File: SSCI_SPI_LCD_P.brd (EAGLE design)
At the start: 114 x 100 mm, 116 parts, among them IC13 74LVC541_RGY, IC18 74LVC541_RGY, IC3 74LVC541_RGY, IC8 74LVC541_RGY, X1 TSW-108-02-S-S, X2 TSW-108-02-S-S, X3 TSW-108-02-S-S, X4 TSW-108-02-S-S, X5 TSW-108-02-S-S, X6 TSW-108-02-S-S, X7 TSW-108-02-S-S, X8 TSW-108-02-S-S

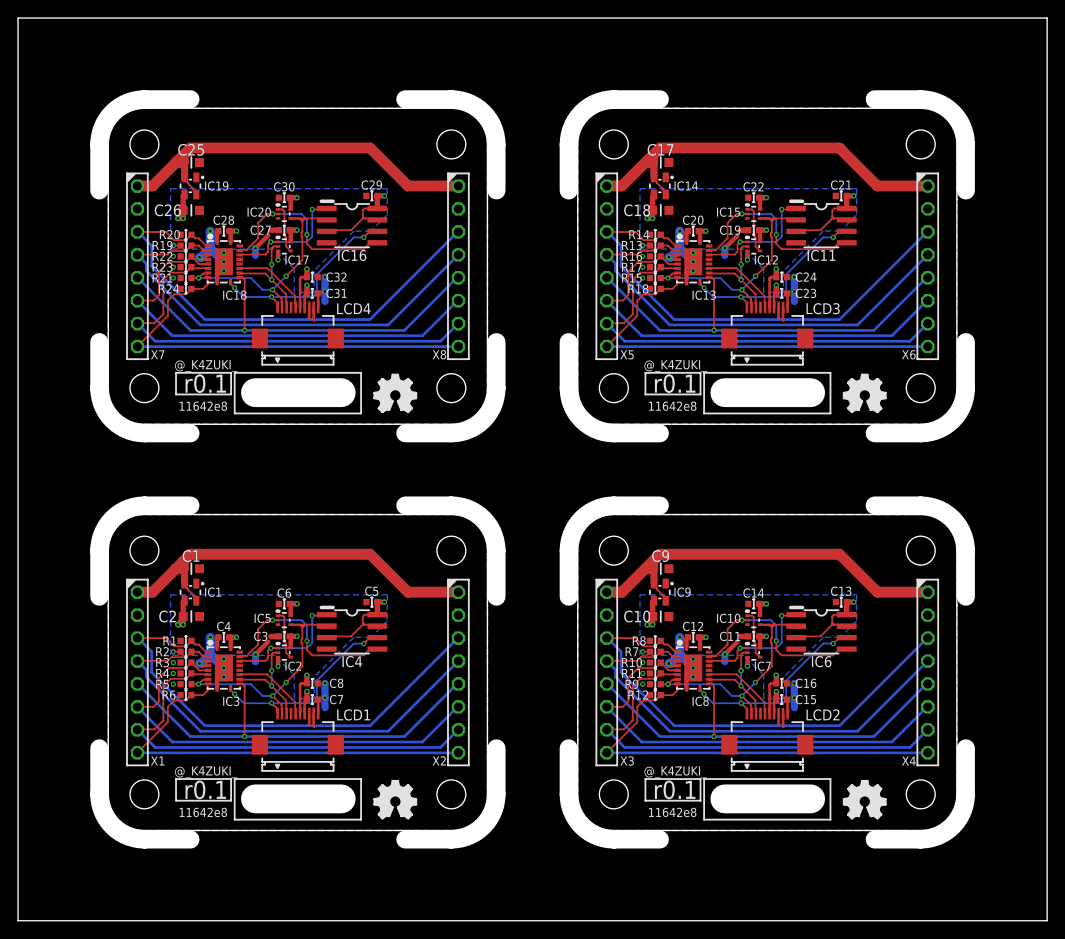
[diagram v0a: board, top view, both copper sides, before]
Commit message: apply changes to panelising file
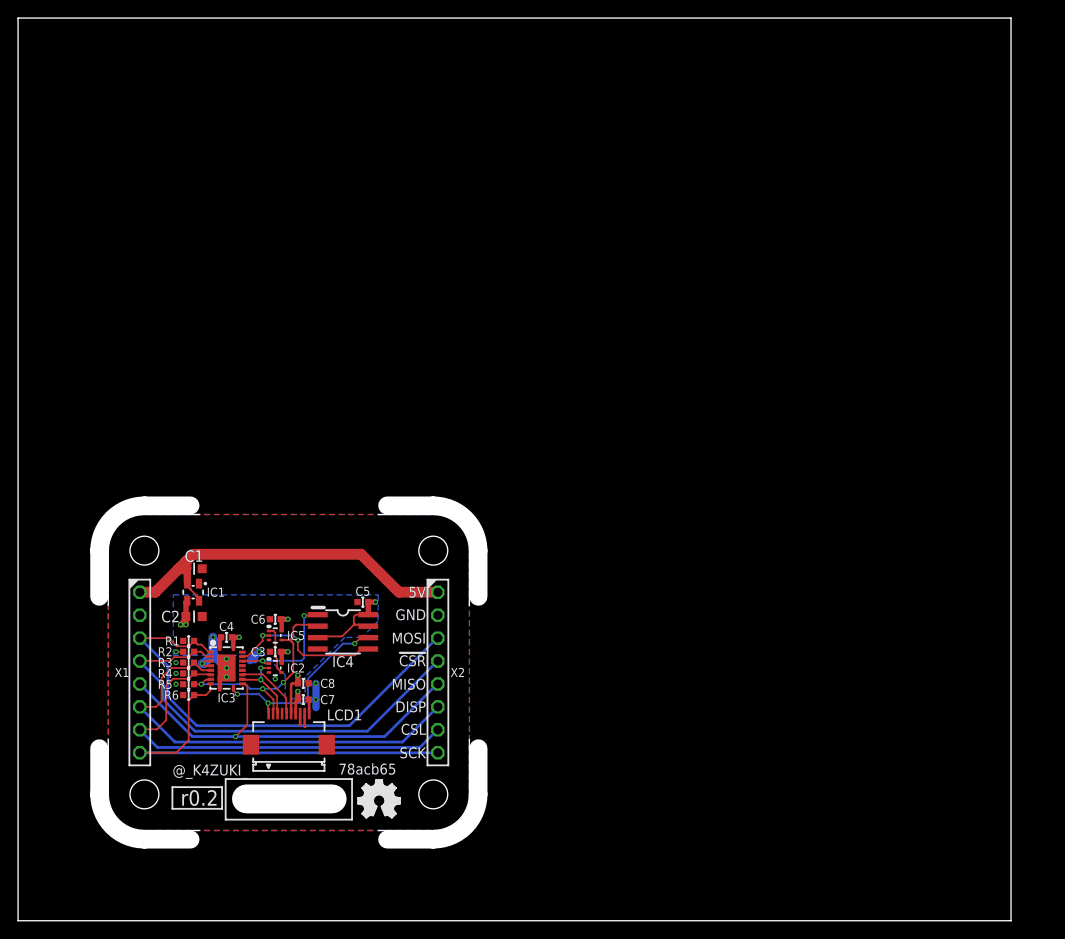
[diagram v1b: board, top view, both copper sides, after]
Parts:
- removed C10, C17, C18, C25, C26, C9: (no value), mylib:CR_1608
- removed C11, C12, C13, C14, C15, C16, C19, C20, C21, C22, C23, C24, C27, C28, C29, C30, C31, C32, R10, R11, R12, R13, R14, R15, R16, R17, R18, R19, R20, R21, R22, R23, R24, R7, R8, R9: (no value), mylib:C0402
- removed GIT2, GIT3, GIT4: 11642e8, git-revision:GIT-REVISION
- removed IC10, IC12, IC15, IC17, IC20, IC7: (no value), mylib:SOT50P160X120-5N
- removed IC11, IC16, IC6: (no value), mylib:IC_08_1.27_150MIL
- removed IC13, IC18, IC8: 74LVC541_RGY, mylib:QFN50P460X360-20N
- removed IC14, IC19, IC9: (no value), mylib:SOT130P220X135-4N
- removed ICON3, ICON5, ICON7: r0.1, mylib:ICON_REVISION2.0
- removed ICON4, ICON6, ICON8: (no value), mylib:ICON_OSHW
- removed LCD2, LCD3, LCD4: LCD_GLCD_400X240, mylib:LCD_GLCD_400X240
- removed P10, P11, P12, P13, P14, P15, P16, P5, P6, P7, P8, P9: (no value), mylib:PCB_CORNER
- removed X3, X4, X5, X6, X7, X8: TSW-108-02-S-S, con-samtec.local:TSW-108-02-S-S
- GIT1: value 11642e8 -> 78acb65; device git-revision:GIT-REVISION -> git-revision:GIT-REVISION_1.2
- ICON1: value r0.1 -> r0.2; device mylib:ICON_REVISION2.0 -> mylib:ICON_REVISION1.7
- moved GIT1 18.8 mm to (38.7, 16.8)
- moved X2 2.27 mm to (46.5, 27.5)
- moved P1 2.00 mm to (46.0, 14.0)
- moved P2 2.00 mm to (46.0, 41.0)
- moved C6 1.97 mm to (28.5, 33.4)
- moved C3 1.97 mm to (28.5, 29.8)
- moved IC2 1.97 mm to (28.5, 28.0)
- moved IC5 1.97 mm to (28.5, 31.6)
- moved ICON2 1.80 mm to (40.0, 13.3)
- moved ICON1 1.08 mm to (20.2, 13.6)
- moved C5 1.00 mm to (38.2, 35.3)
- moved C7 1.00 mm to (31.6, 24.5)
- moved C8 1.00 mm to (31.6, 26.3)
- moved IC4 1.00 mm to (36.0, 32.0)
- moved LCD1 1.00 mm to (30.0, 19.5)
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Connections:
- removed net !CSR!-1: IC6.1, IC7.1, IC8.17
- removed net !CSR!-2: IC11.1, IC12.1, IC13.17
- removed net !CSR!-3: IC16.1, IC17.1, IC18.17
- removed net !CSR!1: IC8.3, R7.2, X3.4, X4.4
- removed net !CSR!2: IC13.3, R13.2, X5.4, X6.4
- removed net !CSR!3: IC18.3, R19.2, X7.4, X8.4
- removed net 3.3V1: C10.1, C11.1, C12.1, C13.1, C14.1, C15.1, C16.1, IC10.5, IC6.3, IC6.7, IC6.8, IC7.5, IC8.20, IC9.3, LCD2.6, LCD2.7, R7.1
- removed net 3.3V2: C18.1, C19.1, C20.1, C21.1, C22.1, C23.1, C24.1, IC11.3, IC11.7, IC11.8, IC12.5, IC13.20, IC14.3, IC15.5, LCD3.6, LCD3.7, R13.1
- removed net 3.3V3: C26.1, C27.1, C28.1, C29.1, C30.1, C31.1, C32.1, IC16.3, IC16.7, IC16.8, IC17.5, IC18.20, IC19.3, IC20.5, LCD4.6, LCD4.7, R19.1
- removed net 5V1: C9.1, IC9.2, IC9.4, X3.1, X4.1
- removed net 5V2: C17.1, IC14.2, IC14.4, X5.1, X6.1
- removed net 5V3: C25.1, IC19.2, IC19.4, X7.1, X8.1
- removed net CSL-1: IC7.2, IC8.13, LCD2.3
- removed net CSL-2: IC12.2, IC13.13, LCD3.3
- removed net CSL-3: IC17.2, IC18.13, LCD4.3
- removed net CSL1: IC8.7, R11.2, X3.7, X4.7
- removed net CSL2: IC13.7, R17.2, X5.7, X6.7
- removed net CSL3: IC18.7, R23.2, X7.7, X8.7
- removed net DISP-1: IC8.14, LCD2.5
- removed net DISP-2: IC13.14, LCD3.5
- removed net DISP-3: IC18.14, LCD4.5
- removed net DISP1: IC8.6, R10.2, X3.6, X4.6
- removed net DISP2: IC13.6, R16.2, X5.6, X6.6
- removed net DISP3: IC18.6, R22.2, X7.6, X8.6
- removed net GND1: C10.2, C11.2, C12.2, C13.2, C14.2, C15.2, C16.2, C9.2, IC10.3, IC6.4, IC7.3, IC8.1, IC8.10, IC8.19, IC8.4, IC8.5, IC8.EP, IC9.1, LCD2.10, LCD2.8, LCD2.9, LCD2.PAD1, LCD2.PAD2, R10.1, R11.1, R12.1, R8.1, R9.1, X3.2, X4.2
- removed net GND2: C17.2, C18.2, C19.2, C20.2, C21.2, C22.2, C23.2, C24.2, IC11.4, IC12.3, IC13.1, IC13.10, IC13.19, IC13.4, IC13.5, IC13.EP, IC14.1, IC15.3, LCD3.10, LCD3.8, LCD3.9, LCD3.PAD1, LCD3.PAD2, R14.1, R15.1, R16.1, R17.1, R18.1, X5.2, X6.2
- removed net GND3: C25.2, C26.2, C27.2, C28.2, C29.2, C30.2, C31.2, C32.2, IC16.4, IC17.3, IC18.1, IC18.10, IC18.19, IC18.4, IC18.5, IC18.EP, IC19.1, IC20.3, LCD4.10, LCD4.8, LCD4.9, LCD4.PAD1, LCD4.PAD2, R20.1, R21.1, R22.1, R23.1, R24.1, X7.2, X8.2
- removed net MISO-1: IC10.4, IC6.2, IC8.8, LCD2.2, R9.2
- removed net MISO-2: IC11.2, IC13.8, IC15.4, LCD3.2, R15.2
- removed net MISO-3: IC16.2, IC18.8, IC20.4, LCD4.2, R21.2
- removed net MISO1: IC8.12, X3.5, X4.5
- removed net MISO2: IC13.12, X5.5, X6.5
- removed net MISO3: IC18.12, X7.5, X8.5
- removed net MOSI-1: IC10.2, IC6.5, IC8.18
- removed net MOSI-2: IC11.5, IC13.18, IC15.2
- removed net MOSI-3: IC16.5, IC18.18, IC20.2
- removed net MOSI1: IC8.2, R8.2, X3.3, X4.3
- removed net MOSI2: IC13.2, R14.2, X5.3, X6.3
- removed net MOSI3: IC18.2, R20.2, X7.3, X8.3
- removed net N$1: IC10.1, IC7.4
- removed net N$3: IC12.4, IC15.1
- removed net N$4: IC17.4, IC20.1
- removed net SCK-1: IC6.6, IC8.11, LCD2.1
- removed net SCK-2: IC11.6, IC13.11, LCD3.1
- removed net SCK-3: IC16.6, IC18.11, LCD4.1
- removed net SCK1: IC8.9, R12.2, X3.8, X4.8
- removed net SCK2: IC13.9, R18.2, X5.8, X6.8
- removed net SCK3: IC18.9, R24.2, X7.8, X8.8
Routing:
- net MOSI1: track 54.0 -> 0.00 mm
- net MOSI3: track 54.0 -> 0.00 mm
- net MOSI2: track 54.0 -> 0.00 mm
- net !CSR!3: track 51.0 -> 0.00 mm
- net !CSR!1: track 51.0 -> 0.00 mm
- net !CSR!2: track 51.0 -> 0.00 mm
- net DISP3: track 50.6 -> 0.00 mm
- net DISP2: track 50.6 -> 0.00 mm
- net DISP1: track 50.6 -> 0.00 mm
- net CSL3: track 50.0 -> 0.00 mm
- net CSL2: track 50.0 -> 0.00 mm
- net CSL1: track 50.0 -> 0.00 mm
- net SCK3: track 48.0 -> 0.00 mm
- net SCK1: track 48.0 -> 0.00 mm
- net SCK2: track 48.0 -> 0.00 mm
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- removed copper zone on layer 16, net 3.3V1
- removed copper zone on layer 16, net 3.3V2
- removed copper zone on layer 16, net 3.3V3
- removed copper zone on layer 1, net GND1
- removed copper zone on layer 16, net GND1
- removed copper zone on layer 1, net GND2
- removed copper zone on layer 16, net GND2
- removed copper zone on layer 1, net GND3
- removed copper zone on layer 16, net GND3
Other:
- board size 114 x 100 mm -> 110 x 100 mm
- board text added: "!CSR!"
- board text added: "5V"
- board text added: "CSL"
- board text added: "DISP"
- board text added: "GND"
- board text added: "MISO"
- board text added: "MOSI"
- board text added: "SCK"
- board text removed: "C1"
- board text removed: "C2"
- board text removed: "C3"
- board text removed: "C4"
- board text removed: "C5"
- board text removed: "C6"
- board text removed: "C7"
- board text removed: "C8"
- board text removed: "IC1"
- board text removed: "IC2"
- board text removed: "IC3"
- board text removed: "IC4"
- board text removed: "IC5"
- board text removed: "LCD1"
- board text removed: "R1"
- board text removed: "R2"
- board text removed: "R3"
- board text removed: "R4"
- board text removed: "R5"
- board text removed: "R6"
- board text removed: "X1"
- board text removed: "X2"

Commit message: update libraries; update panelise; update gerbers
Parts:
- added C10, C17, C18, C25, C26, C9: (no value), mylib:CR_1608
- added C11, C12, C13, C14, C15, C16, C19, C20, C21, C22, C23, C24, C27, C28, C29, C30, C31, C32, R10, R11, R12, R13, R14, R15, R16, R17, R18, R19, R20, R21, R22, R23, R24, R7, R8, R9: (no value), mylib:C0402
- added GIT2, GIT3, GIT4: fd68d81, git-revision:GIT-REVISION_1.2
- added I1, I2, I3, I4: (no value), mylib:ICON_MINLAB_5.2MM
- added IC10, IC12, IC15, IC17, IC20, IC7: (no value), mylib:SOT50P160X120-5N
- added IC11, IC16, IC6: (no value), mylib:IC_08_1.27_150MIL
- added IC13, IC18, IC8: 74LVC541_RGY, mylib:QFN50P460X360-20N
- added IC14, IC19, IC9: (no value), mylib:SOT130P220X135-4N
- added ICON3, ICON5, ICON7: r0.2, mylib:ICON_REVISION1.7
- added ICON4, ICON6, ICON8: (no value), mylib:ICON_OSHW
- added LCD2, LCD3, LCD4: LCD_GLCD_400X240, mylib:LCD_GLCD_400X240
- added P10, P11, P12, P13, P14, P15, P16, P5, P6, P7, P8, P9: (no value), mylib:PCB_CORNER
- added X3, X4, X5, X6, X7, X8: TSW-108-02-S-S, con-samtec.local:TSW-108-02-S-S
- GIT1: value 78acb65 -> fd68d81
- moved ICON1 36.0 mm to (40.5, 43.3)
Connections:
- new net !CSR!-1: IC6.1, IC7.1, IC8.17
- new net !CSR!-2: IC11.1, IC12.1, IC13.17
- new net !CSR!-3: IC16.1, IC17.1, IC18.17
- new net !CSR!1: IC8.3, R7.2, X3.4, X4.4
- new net !CSR!2: IC13.3, R13.2, X5.4, X6.4
- new net !CSR!3: IC18.3, R19.2, X7.4, X8.4
- new net 3.3V1: C10.1, C11.1, C12.1, C13.1, C14.1, C15.1, C16.1, IC10.5, IC6.3, IC6.7, IC6.8, IC7.5, IC8.20, IC9.3, LCD2.6, LCD2.7, R7.1
- new net 3.3V2: C18.1, C19.1, C20.1, C21.1, C22.1, C23.1, C24.1, IC11.3, IC11.7, IC11.8, IC12.5, IC13.20, IC14.3, IC15.5, LCD3.6, LCD3.7, R13.1
- new net 3.3V3: C26.1, C27.1, C28.1, C29.1, C30.1, C31.1, C32.1, IC16.3, IC16.7, IC16.8, IC17.5, IC18.20, IC19.3, IC20.5, LCD4.6, LCD4.7, R19.1
- new net 5V1: C9.1, IC9.2, IC9.4, X3.1, X4.1
- new net 5V2: C17.1, IC14.2, IC14.4, X5.1, X6.1
- new net 5V3: C25.1, IC19.2, IC19.4, X7.1, X8.1
- new net CSL-1: IC7.2, IC8.13, LCD2.3
- new net CSL-2: IC12.2, IC13.13, LCD3.3
- new net CSL-3: IC17.2, IC18.13, LCD4.3
- new net CSL1: IC8.7, R11.2, X3.7, X4.7
- new net CSL2: IC13.7, R17.2, X5.7, X6.7
- new net CSL3: IC18.7, R23.2, X7.7, X8.7
- new net DISP-1: IC8.14, LCD2.5
- new net DISP-2: IC13.14, LCD3.5
- new net DISP-3: IC18.14, LCD4.5
- new net DISP1: IC8.6, R10.2, X3.6, X4.6
- new net DISP2: IC13.6, R16.2, X5.6, X6.6
- new net DISP3: IC18.6, R22.2, X7.6, X8.6
- new net GND1: C10.2, C11.2, C12.2, C13.2, C14.2, C15.2, C16.2, C9.2, IC10.3, IC6.4, IC7.3, IC8.1, IC8.10, IC8.19, IC8.4, IC8.5, IC8.EP, IC9.1, LCD2.10, LCD2.8, LCD2.9, LCD2.PAD1, LCD2.PAD2, R10.1, R11.1, R12.1, R8.1, R9.1, X3.2, X4.2
- new net GND2: C17.2, C18.2, C19.2, C20.2, C21.2, C22.2, C23.2, C24.2, IC11.4, IC12.3, IC13.1, IC13.10, IC13.19, IC13.4, IC13.5, IC13.EP, IC14.1, IC15.3, LCD3.10, LCD3.8, LCD3.9, LCD3.PAD1, LCD3.PAD2, R14.1, R15.1, R16.1, R17.1, R18.1, X5.2, X6.2
- new net GND3: C25.2, C26.2, C27.2, C28.2, C29.2, C30.2, C31.2, C32.2, IC16.4, IC17.3, IC18.1, IC18.10, IC18.19, IC18.4, IC18.5, IC18.EP, IC19.1, IC20.3, LCD4.10, LCD4.8, LCD4.9, LCD4.PAD1, LCD4.PAD2, R20.1, R21.1, R22.1, R23.1, R24.1, X7.2, X8.2
- new net MISO-1: IC10.4, IC6.2, IC8.8, LCD2.2, R9.2
- new net MISO-2: IC11.2, IC13.8, IC15.4, LCD3.2, R15.2
- new net MISO-3: IC16.2, IC18.8, IC20.4, LCD4.2, R21.2
- new net MISO1: IC8.12, X3.5, X4.5
- new net MISO2: IC13.12, X5.5, X6.5
- new net MISO3: IC18.12, X7.5, X8.5
- new net MOSI-1: IC10.2, IC6.5, IC8.18
- new net MOSI-2: IC11.5, IC13.18, IC15.2
- new net MOSI-3: IC16.5, IC18.18, IC20.2
- new net MOSI1: IC8.2, R8.2, X3.3, X4.3
- new net MOSI2: IC13.2, R14.2, X5.3, X6.3
- new net MOSI3: IC18.2, R20.2, X7.3, X8.3
- new net N$1: IC10.1, IC7.4
- new net N$3: IC12.4, IC15.1
- new net N$4: IC17.4, IC20.1
- new net SCK-1: IC6.6, IC8.11, LCD2.1
- new net SCK-2: IC11.6, IC13.11, LCD3.1
- new net SCK-3: IC16.6, IC18.11, LCD4.1
- new net SCK1: IC8.9, R12.2, X3.8, X4.8
- new net SCK2: IC13.9, R18.2, X5.8, X6.8
- new net SCK3: IC18.9, R24.2, X7.8, X8.8
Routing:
- net MOSI3: track 0.00 -> 52.1 mm
- net MOSI2: track 0.00 -> 52.1 mm
- net MOSI1: track 0.00 -> 52.1 mm
- net !CSR!1: track 0.00 -> 48.9 mm
- net !CSR!3: track 0.00 -> 48.9 mm
- net !CSR!2: track 0.00 -> 48.9 mm
- net DISP3: track 0.00 -> 48.0 mm
- net DISP1: track 0.00 -> 48.0 mm
- net DISP2: track 0.00 -> 48.0 mm
- net CSL2: track 0.00 -> 47.4 mm
- net CSL3: track 0.00 -> 47.4 mm
- net CSL1: track 0.00 -> 47.4 mm
- net SCK2: track 0.00 -> 47.0 mm
- net SCK3: track 0.00 -> 47.0 mm
- net SCK1: track 0.00 -> 47.0 mm
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- added copper zone on layer 16, net 3.3V1
- added copper zone on layer 16, net 3.3V2
- added copper zone on layer 16, net 3.3V3
- added copper zone on layer 1, net GND1
- added copper zone on layer 16, net GND1
- added copper zone on layer 1, net GND2
- added copper zone on layer 16, net GND2
- added copper zone on layer 1, net GND3
- added copper zone on layer 16, net GND3
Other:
- board text added: "C1"
- board text added: "C2"
- board text added: "C3"
- board text added: "C4"
- board text added: "C5"
- board text added: "C6"
- board text added: "C7"
- board text added: "C8"
- board text added: "IC1"
- board text added: "IC2"
- board text added: "IC3"
- board text added: "IC4"
- board text added: "IC5"
- board text added: "LCD1"
- board text added: "R1"
- board text added: "R2"
- board text added: "R3"
- board text added: "R4"
- board text added: "R5"
- board text added: "R6"
- board text added: "X1"
- board text added: "X2"

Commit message: [ BRD ] panelized
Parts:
- added TP1, TP2, TP3: (no value), mylib:FIDUCIAL
- GIT1, GIT2, GIT3, GIT4: value fd68d81 -> fcf31d8
- ICON1, ICON3, ICON5, ICON7: value r0.2 -> r0.3
- X1, X2, X3, X4, X5, X6, X7, X8: value TSW-108-02-S-S -> PHA-1X08SG; device con-samtec.local:TSW-108-02-S-S -> mylib:PHA-1X08SG
- moved ICON7 50.5 mm to (40.0, 87.8)
- moved I3 50.0 mm to (67.4, 56.0)
- moved I4 50.0 mm to (17.4, 56.0)
- moved IC14 50.0 mm to (69.4, 81.4)
- moved IC19 50.0 mm to (19.4, 81.4)
- moved R13 50.0 mm to (68.9, 74.8)
- moved R14 50.0 mm to (68.9, 76.0)
- moved R15 50.0 mm to (68.9, 71.2)
- moved R16 50.0 mm to (68.9, 73.6)
- moved R17 50.0 mm to (68.9, 72.4)
- moved R18 50.0 mm to (68.9, 70.0)
- moved R19 50.0 mm to (18.9, 74.8)
- moved R20 50.0 mm to (18.9, 76.0)
- moved R21 50.0 mm to (18.9, 71.2)
- moved R22 50.0 mm to (18.9, 73.6)
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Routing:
- net GND3: track 22.4 -> 26.4 mm, vias 12 -> 13
- net GND1: track 22.4 -> 26.4 mm, vias 12 -> 13
- net GND: track 22.4 -> 26.4 mm, vias 12 -> 13
- net GND2: track 22.4 -> 26.4 mm, vias 12 -> 13

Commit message: 8c37b00 panelized
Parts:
- added C33, C34, C41, C42: (no value), mylib:CR_1608
- added C35, C36, C37, C38, C39, C40, C43, C44, C45, C46, C47, C48, R25, R26, R27, R28, R29, R30, R31, R32, R33, R34, R35, R36: (no value), mylib:C0402
- added GIT5, GIT6: 8c37b00, git-revision:GIT-REVISION_1.2
- added I5, I6: (no value), mylib:ICON_MINLAB_5.2MM
- added IC21, IC26: (no value), mylib:IC_08_1.27_150MIL
- added IC22, IC25, IC27, IC30: (no value), mylib:SOT50P160X120-5N
- added IC23, IC28: 74LVC541_RGY, mylib:QFN50P460X360-20N
- added IC24, IC29: (no value), mylib:SOT130P220X135-4N
- added ICON10, ICON12: (no value), mylib:ICON_OSHW
- added ICON11, ICON9: r0.3, mylib:ICON_REVISION1.7
- added LCD5, LCD6: LCD_GLCD_400X240, mylib:LCD_GLCD_400X240
- added P17, P18, P19, P20, P21, P22, P23, P24: (no value), mylib:PCB_CORNER_NH
- added X10, X11, X12, X9: PHA-1X08SG, mylib:PHA-1X08SG
- GIT1, GIT2, GIT3, GIT4: value fcf31d8 -> 8c37b00
- P1, P10, P11, P12, P13, P14, P15, P16, P2, P3, P4, P5, P6, P7, P8, P9: device mylib:PCB_CORNER -> mylib:PCB_CORNER_NH
- moved ICON3 77.5 mm to (26.9, 87.8)
- moved P5 77.4 mm to (33.0, 59.0)
- moved P6 77.4 mm to (33.0, 86.0)
- moved X4 76.2 mm to (35.0, 72.5)
- moved C10 74.2 mm to (10.5, 78.7)
- moved C11 74.2 mm to (19.5, 74.8)
- moved C13 74.2 mm to (29.2, 80.3)
- moved C14 74.2 mm to (19.5, 78.4)
- moved C9 74.2 mm to (10.5, 84.0)
- moved GIT2 74.2 mm to (29.7, 61.8)
- moved IC6 74.2 mm to (27.0, 77.0)
- moved IC7 74.2 mm to (19.5, 73.0)
- moved IC9 74.2 mm to (10.4, 81.4)
- moved ICON4 74.2 mm to (31.0, 58.3)
- moved LCD2 74.2 mm to (21.0, 64.5)
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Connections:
- new net !CSR!-4: IC21.1, IC22.1, IC23.17
- new net !CSR!-5: IC26.1, IC27.1, IC28.17
- new net !CSR!4: IC23.3, R25.2, X10.4, X9.4
- new net !CSR!5: IC28.3, R31.2, X11.4, X12.4
- new net 3.3V4: C34.1, C35.1, C36.1, C37.1, C38.1, C39.1, C40.1, IC21.3, IC21.7, IC21.8, IC22.5, IC23.20, IC24.3, IC25.5, LCD5.6, LCD5.7, R25.1, R28.1
- new net 3.3V5: C42.1, C43.1, C44.1, C45.1, C46.1, C47.1, C48.1, IC26.3, IC26.7, IC26.8, IC27.5, IC28.20, IC29.3, IC30.5, LCD6.6, LCD6.7, R31.1, R34.1
- new net 5V4: C33.1, IC24.2, IC24.4, X10.1, X9.1
- new net 5V5: C41.1, IC29.2, IC29.4, X11.1, X12.1
- new net CSL-4: IC22.2, IC23.13, LCD5.3
- new net CSL-5: IC27.2, IC28.13, LCD6.3
- new net CSL4: IC23.7, R29.2, X10.7, X9.7
- new net CSL5: IC28.7, R35.2, X11.7, X12.7
- new net DISP-4: IC23.14, LCD5.5
- new net DISP-5: IC28.14, LCD6.5
- new net DISP4: IC23.6, R28.2, X10.6, X9.6
- new net DISP5: IC28.6, R34.2, X11.6, X12.6
- new net GND4: C33.2, C34.2, C35.2, C36.2, C37.2, C38.2, C39.2, C40.2, IC21.4, IC22.3, IC23.1, IC23.10, IC23.19, IC23.4, IC23.5, IC23.EP, IC24.1, IC25.3, LCD5.10, LCD5.8, LCD5.9, LCD5.PAD1, LCD5.PAD2, R26.1, R27.1, R29.1, R30.1, X10.2, X9.2
- new net GND5: C41.2, C42.2, C43.2, C44.2, C45.2, C46.2, C47.2, C48.2, IC26.4, IC27.3, IC28.1, IC28.10, IC28.19, IC28.4, IC28.5, IC28.EP, IC29.1, IC30.3, LCD6.10, LCD6.8, LCD6.9, LCD6.PAD1, LCD6.PAD2, R32.1, R33.1, R35.1, R36.1, X11.2, X12.2
- new net MISO-4: IC21.2, IC23.8, IC25.4, LCD5.2, R27.2
- new net MISO-5: IC26.2, IC28.8, IC30.4, LCD6.2, R33.2
- new net MISO4: IC23.12, X10.5, X9.5
- new net MISO5: IC28.12, X11.5, X12.5
- new net MOSI-4: IC21.5, IC23.18, IC25.2
- new net MOSI-5: IC26.5, IC28.18, IC30.2
- new net MOSI4: IC23.2, R26.2, X10.3, X9.3
- new net MOSI5: IC28.2, R32.2, X11.3, X12.3
- new net N$5: IC22.4, IC25.1
- new net N$6: IC27.4, IC30.1
- new net SCK-4: IC21.6, IC23.11, LCD5.1
- new net SCK-5: IC26.6, IC28.11, LCD6.1
- new net SCK4: IC23.9, R30.2, X10.8, X9.8
- new net SCK5: IC28.9, R36.2, X11.8, X12.8
- net 3.3V: now also R3.1
- net 3.3V1: now also R10.1
- net 3.3V2: now also R16.1
- net 3.3V3: now also R22.1
- net GND: no longer R3.1
- net GND1: no longer R10.1
- net GND2: no longer R16.1
- net GND3: no longer R22.1
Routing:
- net MOSI5: track 0.00 -> 46.3 mm
- net MOSI4: track 0.00 -> 46.3 mm
- net !CSR!5: track 0.00 -> 42.9 mm
- net !CSR!4: track 0.00 -> 42.9 mm
- net DISP5: track 0.00 -> 41.7 mm
- net DISP4: track 0.00 -> 41.7 mm
- net CSL4: track 0.00 -> 41.3 mm
- net CSL5: track 0.00 -> 41.3 mm
- net SCK5: track 0.00 -> 40.9 mm
- net SCK4: track 0.00 -> 40.9 mm
- net MISO5: track 0.00 -> 40.3 mm, vias 0 -> 1
- net MISO4: track 0.00 -> 40.3 mm, vias 0 -> 1
- net 5V5: track 0.00 -> 38.9 mm
- net 5V4: track 0.00 -> 38.9 mm
- net 3.3V4: track 0.00 -> 32.9 mm, vias 0 -> 10
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- added copper zone on layer 16, net 3.3V4
- added copper zone on layer 16, net 3.3V5
- added copper zone on layer 1, net GND4
- added copper zone on layer 16, net GND4
- added copper zone on layer 1, net GND5
- added copper zone on layer 16, net GND5
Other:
- outline, holes or cut-outs redrawn
